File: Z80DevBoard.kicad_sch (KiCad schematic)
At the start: 83 parts, among them SW1 WAIT, SW2 RESET, SW3 Z80BOOT, SW4 RPBOOT

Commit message: Added the read data from ram hardware. Added resistors for leds and some diodes. Reorganized the spaces.
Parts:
- removed ShiftRegisterIn: 74HC165, symbol 74xx:74HC165
- added D11, D13, D15, D17, D19, D21, D23, D25, D27, D29, D3, D46, D5, D54, D56, D58, D59, D60, D61, D62, D63, D64, D7, D9: Diode, Diode_SMD:D_SOD-523, symbol Diode:1N4148WT
- added DataBus1, DataBus2: SN74LVC245APW, Package_SO:TSSOP-20_4.4x6.5mm_P0.65mm, symbol Logic_LevelTranslator:SN74LVC245APW
- added R19, R20, R21, R22, R23, R24, R25, R26, R27, R28, R29, R30, R31, R32, R33, R34, R35, R36, R37, R38, R39, R40, R41, R42, R43, R44, R45, R46, R47, R48, R49, R50, R51, R52: 220, Resistor_THT:R_Axial_DIN0207_L6.3mm_D2.5mm_P10.16mm_Horizontal, symbol Device:R
- added ShiftRegisterIn2: 74HC165, symbol 74xx:74HC165
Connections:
- net GND: now also DataBus1.10 (GND), DataBus2.10 (GND), ShiftRegisterIn2.8 (GND)
- net RAM-A0: now also DataBus.18 (B1)
- net RAM-A1: now also DataBus.17 (B2)
- net RAM-A10: now also DataBus1.16 (B3)
- net RAM-A11: now also DataBus1.15 (B4)
- net RAM-A12: now also DataBus1.14 (B5)
- net RAM-A13: now also DataBus1.13 (B6)
- net RAM-A14: now also DataBus1.12 (B7)
- net RAM-A2: now also DataBus.16 (B3)
- net RAM-A3: now also DataBus.15 (B4)
- net RAM-A4: now also DataBus.14 (B5)
- net RAM-A5: now also DataBus.13 (B6)
- net RAM-A6: now also DataBus.12 (B7)
- net RAM-A7: now also DataBus.11 (B8)
- net RAM-A8: now also DataBus1.18 (B1)
- net RAM-A9: now also DataBus1.17 (B2)
- net RAM-Q0: now also DataBus2.18 (B1), R22.2; no longer D31.2 (A), D32.1 (K)
- net RAM-Q1: now also DataBus2.17 (B2), R29.2; no longer D35.2 (A), D36.1 (K)
- net RAM-Q2: now also DataBus2.16 (B3), R30.2; no longer D39.2 (A), D40.1 (K)
- net RAM-Q3: now also DataBus2.15 (B4), R35.2; no longer D43.2 (A), D44.1 (K)
- net RAM-Q4: now also DataBus2.14 (B5), R23.2; no longer D47.2 (A), D48.1 (K)
- net RAM-Q5: now also DataBus2.13 (B6), R28.2; no longer D33.2 (A), D34.1 (K)
- net RAM-Q6: now also DataBus2.12 (B7), R31.2; no longer D37.2 (A), D38.1 (K)
- net RAM-Q7: now also DataBus2.11 (B8), R34.2; no longer D41.2 (A), D42.1 (K)
- net Vcc: now also DataBus1.20 (VCC), DataBus2.20 (VCC)
- net Vdd_3v3: now also ShiftRegisterIn2.16 (VCC)
- net Z80-A0: now also R40.2; no longer D8.2 (A)
- net Z80-A1: now also R41.2; no longer D22.2 (A)
- net Z80-A10: now also R38.2; no longer D12.2 (A)
- net Z80-A11: now also R43.2; no longer D14.2 (A)
- net Z80-A12: now also R46.2; no longer D16.2 (A)
- net Z80-A13: now also R49.2; no longer D18.2 (A)
- net Z80-A14: now also R52.2; no longer D20.2 (A)
- net Z80-A15: now also R19.1; no longer D57.2 (A)
- net Z80-A2: now also R44.2; no longer D26.2 (A)
- net Z80-A3: now also R47.2; no longer D28.2 (A)
- net Z80-A4: now also R50.2; no longer D30.2 (A)
- net Z80-A5: now also R39.2; no longer D10.2 (A)
- net Z80-A6: now also R42.2; no longer D2.2 (A)
- net Z80-A7: now also R45.2; no longer D4.2 (A)
- net Z80-A8: now also R48.2; no longer D6.2 (A)
- net Z80-A9: now also R51.2; no longer D24.2 (A)
- net Z80-D0: now also R25.1; no longer D31.1 (K), D32.2 (A)
- net Z80-D1: now also R26.1; no longer D35.1 (K), D36.2 (A)
- net Z80-D2: now also R32.1; no longer D39.1 (K), D40.2 (A)
- net Z80-D3: now also R36.1; no longer D43.1 (K), D44.2 (A)
- net Z80-D4: now also R24.1; no longer D47.1 (K), D48.2 (A)
- net Z80-D5: now also R27.1; no longer D33.1 (K), D34.2 (A)
- net Z80-D6: now also R33.1; no longer D37.1 (K), D38.2 (A)
- net Z80-D7: now also R37.1; no longer D41.1 (K), D42.2 (A)
- net Z80-RD: now also R20.1; no longer D49.2 (A)
- net Z80-WR: now also R21.1; no longer D55.2 (A)
- net at ShiftRegisterOut.1 (QB): now also D5.2 (A)
- net at ShiftRegisterOut.15 (QA): now also D3.2 (A)
- net at ShiftRegisterOut.2 (QC): now also D7.2 (A)
- net at ShiftRegisterOut.3 (QD): now also D9.2 (A)
- net at ShiftRegisterOut.4 (QE): now also D11.2 (A)
- net at ShiftRegisterOut.5 (QF): now also D13.2 (A)
- net at ShiftRegisterOut.6 (QG): now also D15.2 (A)
- net at ShiftRegisterOut.7 (QH): now also D17.2 (A)
- net at ShiftRegisterOut2.1 (QB): now also D61.2 (A)
- net at ShiftRegisterOut2.15 (QA): now also D56.2 (A)
- net at ShiftRegisterOut2.2 (QC): now also D58.2 (A)
- net at ShiftRegisterOut2.3 (QD): now also D62.2 (A)
- net at ShiftRegisterOut2.4 (QE): now also D59.2 (A)
- net at ShiftRegisterOut2.5 (QF): now also D63.2 (A)
- net at ShiftRegisterOut2.6 (QG): now also D60.2 (A)
- net at ShiftRegisterOut2.7 (QH): now also D64.2 (A)
- net at DataBus.2 (A1): now also D3.1 (K)
- net at DataBus.3 (A2): now also D5.1 (K)
- net at DataBus.4 (A3): now also D7.1 (K)
- net at DataBus.5 (A4): now also D9.1 (K)
- net at DataBus.6 (A5): now also D11.1 (K)
- net at DataBus.7 (A6): now also D13.1 (K)
- net at DataBus.8 (A7): now also D15.1 (K)
- net at DataBus.9 (A8): now also D17.1 (K)
- net at ShiftRegisterOut1.1 (QB): now also D27.2 (A)
- net at ShiftRegisterOut1.15 (QA): now also D19.2 (A)
- net at ShiftRegisterOut1.2 (QC): now also D21.2 (A)
- net at ShiftRegisterOut1.3 (QD): now also D29.2 (A)
- net at ShiftRegisterOut1.4 (QE): now also D23.2 (A)
- net at ShiftRegisterOut1.5 (QF): now also D46.2 (A)
- net at ShiftRegisterOut1.6 (QG): now also D25.2 (A)
- net at ShiftRegisterOut1.7 (QH): now also D54.2 (A)
- new net: D30.2 (A), R50.1
- new net: D19.1 (K), DataBus1.2 (A1)
- new net: D27.1 (K), DataBus1.3 (A2)
- new net: D21.1 (K), DataBus1.4 (A3)
- new net: D29.1 (K), DataBus1.5 (A4)
- new net: D23.1 (K), DataBus1.6 (A5)
- new net: D46.1 (K), DataBus1.7 (A6)
- new net: D25.1 (K), DataBus1.8 (A7)
- new net: D54.1 (K), DataBus1.9 (A8)
- new net: D37.2 (A), D38.1 (K), R31.1
- new net: D47.2 (A), D48.1 (K), R23.1
- new net: D43.2 (A), D44.1 (K), R35.1
- new net: D31.1 (K), D32.2 (A), R25.2
- new net: D31.2 (A), D32.1 (K), R22.1
- new net: D2.2 (A), R42.1
- new net: D28.2 (A), R47.1
- new net: D61.1 (K), DataBus2.3 (A2), ShiftRegisterIn2.12 (D1)
- new net: D41.1 (K), D42.2 (A), R37.2
- new net: D58.1 (K), DataBus2.4 (A3), ShiftRegisterIn2.13 (D2)
- new net: D56.1 (K), DataBus2.2 (A1), ShiftRegisterIn2.11 (D0)
- new net: D62.1 (K), DataBus2.5 (A4), ShiftRegisterIn2.14 (D3)
- new net: D59.1 (K), DataBus2.6 (A5), ShiftRegisterIn2.3 (D4)
- new net: D63.1 (K), DataBus2.7 (A6), ShiftRegisterIn2.4 (D5)
- new net: D60.1 (K), DataBus2.8 (A7), ShiftRegisterIn2.5 (D6)
- new net: D64.1 (K), DataBus2.9 (A8), ShiftRegisterIn2.6 (D7)
- new net: D39.1 (K), D40.2 (A), R32.2
- new net: D41.2 (A), D42.1 (K), R34.1
- new net: D26.2 (A), R44.1
- new net: D33.1 (K), D34.2 (A), R27.2
- new net: D33.2 (A), D34.1 (K), R28.1
- new net: D22.2 (A), R41.1
- new net: D24.2 (A), R51.1
- new net: D49.2 (A), R20.2
- new net: D37.1 (K), D38.2 (A), R33.2
- new net: D47.1 (K), D48.2 (A), R24.2
- new net: D8.2 (A), R40.1
- new net: D20.2 (A), R52.1
- new net: D4.2 (A), R45.1
- new net: D6.2 (A), R48.1
- new net: D55.2 (A), R21.2
- new net: D14.2 (A), R43.1
- new net: D39.2 (A), D40.1 (K), R30.1
- new net: D43.1 (K), D44.2 (A), R36.2
- new net: D12.2 (A), R38.1
- new net: D18.2 (A), R49.1
- new net: D10.2 (A), R39.1
- new net: D35.1 (K), D36.2 (A), R26.2
- new net: D35.2 (A), D36.1 (K), R29.1
- new net: D57.2 (A), R19.2
- new net: D16.2 (A), R46.1
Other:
- moved on the sheet: C3, C4, C5, C6, C7, C8, D1, D10, D12, D14, D16, D18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

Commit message: Added some footprints. Made the connections between the shift register and the RP2040.
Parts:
- C1, C2, C3, C4, C5, C6, C7, C8: footprint (none) -> Capacitor_SMD:CP_Elec_3x5.3
- F1: footprint (none) -> Fuse:Fuse_0402_1005Metric
- USB_C1: renamed from USB_C; footprint (none) -> Connector_USB:USB_C_Receptacle_Amphenol_124019772112A
- renumbered DataBus to DataBus3, LDO to LDO1, ShiftRegisterOut to ShiftRegisterOut3
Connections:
- net CLOCK: now also ShiftRegisterIn2.2 (CP)
- net GND: now also DataBus1.19 (~{OE}), DataBus2.19 (~{OE}), DataBus3.19 (~{OE}), ShiftRegisterIn2.15 (~{CE})
- net Vcc: now also DataBus1.1 (DIR), DataBus3.1 (DIR)
- net RP2040-RWRAM-GPIO5-DIR: now reaches DataBus2.1 (DIR)
- net RP2040-RWRAM-GPIO5-DIR: now also RP2040_1.7 (GPIO5)
- net RP2040-RWRAM-GPIO8-PL: now reaches RP2040_1.11 (GPIO8)
- net RP2040-RWRAM-GPIO8-PL: now also ShiftRegisterIn2.1 (~{PL})
- net RP2040-RWRAM-GPIO6-DS: now reaches RP2040_1.8 (GPIO6)
- net RP2040-RWRAM-GPIO6-DS: now also ShiftRegisterIn2.10 (DS)
- net RP2040-RWRAM-GPIO7-Q7: now reaches RP2040_1.9 (GPIO7)
- net RP2040-RWRAM-GPIO7-Q7: now also ShiftRegisterIn2.9 (Q7)
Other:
- moved on the sheet: RP2040_1

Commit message: Added the last footprints.
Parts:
- ShiftRegisterIn2, ShiftRegisterOut1, ShiftRegisterOut2, ShiftRegisterOut3: footprint (none) -> Package_DIP:DIP-16_W7.62mm
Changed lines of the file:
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@@
 			)
 		)
-		(property "Footprint" ""
+		(property "Footprint" "Package_DIP:DIP-16_W7.62mm"
 			(at 441.96 53.34 0)
 			(effects
@@
 			)
 		)
-		(property "Footprint" ""
+		(property "Footprint" "Package_DIP:DIP-16_W7.62mm"
 			(at 441.96 198.12 0)
 			(effects
@@
 			)
 		)
-		(property "Footprint" ""
+		(property "Footprint" "Package_DIP:DIP-16_W7.62mm"
 			(at 441.96 125.73 0)
 			(effects
@@
 			)
 		)
-		(property "Footprint" ""
+		(property "Footprint" "Package_DIP:DIP-16_W7.62mm"
 			(at 502.92 200.66 0)
 			(effects

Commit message: Updated the USB C port.
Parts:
- USB_C1: footprint Connector_USB:USB_C_Receptacle_Amphenol_124019772112A -> Connector_USB:USB_C_Receptacle_GCT_USB4085
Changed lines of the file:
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@@
 			)
 		)
-		(property "Footprint" "Connector_USB:USB_C_Receptacle_Amphenol_124019772112A"
+		(property "Footprint" "Connector_USB:USB_C_Receptacle_GCT_USB4085"
 			(at 528.32 344.17 0)
 			(effects

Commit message: Fixed the oscillators. Fixed the crystal. Fixed the connections between the RP2040 and the Flash. Updated README.
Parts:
- removed R16: 10k, Resistor_THT:R_Axial_DIN0207_L6.3mm_D2.5mm_P10.16mm_Horizontal, symbol Device:R
- added C10, C12, C9: 0.1uF, Capacitor_SMD:CP_Elec_3x5.3, symbol Device:C
- added C11: 12pF, Capacitor_SMD:CP_Elec_3x5.3, symbol Device:C
- added J1: Conn_01x02_MountingPin, Connector_PinHeader_1.00mm:PinHeader_1x02_P1.00mm_Vertical, symbol Connector_Generic_MountingPin:Conn_01x02_MountingPin
- added O2: 10KHz, Oscillator:Oscillator_SMD_SeikoEpson_SG210-4Pin_2.5x2.0mm, symbol Device:Oscilloscope
- added Y1: Crystal, Crystal:Crystal_HC49-4H_Vertical, symbol Device:Crystal
- C8: value 0.1uF -> 12pF
- O1: value 6MHz -> 10KHz; footprint Crystal:Crystal_HC49-4H_Vertical -> Oscillator:Oscillator_SMD_SeikoEpson_SG210-4Pin_2.5x2.0mm
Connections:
- net FLASH-HOLD/RESET is gone; now on net FLASH-HOLD-RESRT-RP2040-QSPI_SD3: Flash1.7 (~{HOLD}/~{RESET}/IO_{3})
- net GND: now also C11.1, C12.1, C9.1, J1.MP (MountPin)
- net Vdd_3v3: now also C10.2, C12.2, C9.2, O2.2 (+); no longer C8.2
- net RP2040_XOUT: now reaches RP2040_1.21 (XOUT)
- net RP2040_XOUT: now also C11.2, Y1.2
- net RP2040-SWCLK-PIN: now reaches RP2040_1.24 (SWCLK)
- net RP2040-SWCLK-PIN: now also J1.1 (Pin_1)
- net RP2040-SWD-PIN: now reaches RP2040_1.25 (SWD)
- net RP2040-SWD-PIN: now also J1.2 (Pin_2)
- net Vcc-RP2040-RUN: now reaches RP2040_1.26 (RUN)
- net Vcc-RP2040-RUN: now also R15.1
- net RP2040-VREG_IN: now reaches RP2040_1.44 (VREG_IN)
- net RP2040-VREG_IN: now also C10.1
- net FLASH-HOLD-RESRT-RP2040-QSPI_SD3: now reaches RP2040_1.51 (QSPI_SD3)
- net FLASH-WP-RP2040-QSPI_SD2: now reaches RP2040_1.54 (QSPI_SD2)
- net FLASH-WP-RP2040-QSPI_SD2: now also Flash1.3 (~{WP}/IO_{2})
- net CLOCK renamed CLOCK_BUS
- net CLOCK_BUS: no longer Flash1.6 (CLK), RP2040_1.20 (XIN), RP2040_1.52 (QSPI_SCLK), Z80.6 (CLK)
- removed net FLASH-WP: Flash1.3 (~{WP}/IO_{2}), R15.1
- new net CLOCK_FLASH: Flash1.6 (CLK), RP2040_1.52 (QSPI_SCLK)
- new net CLOCK_Z80: O2.1 (-), Z80.6 (CLK)
- new net RP2040_XIN: C8.2, RP2040_1.20 (XIN), Y1.1
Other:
- note added: "Pins"
- moved on the sheet: C3, C4, C5, C6, C8, R1, R12, R13, R2, R3, RAM1

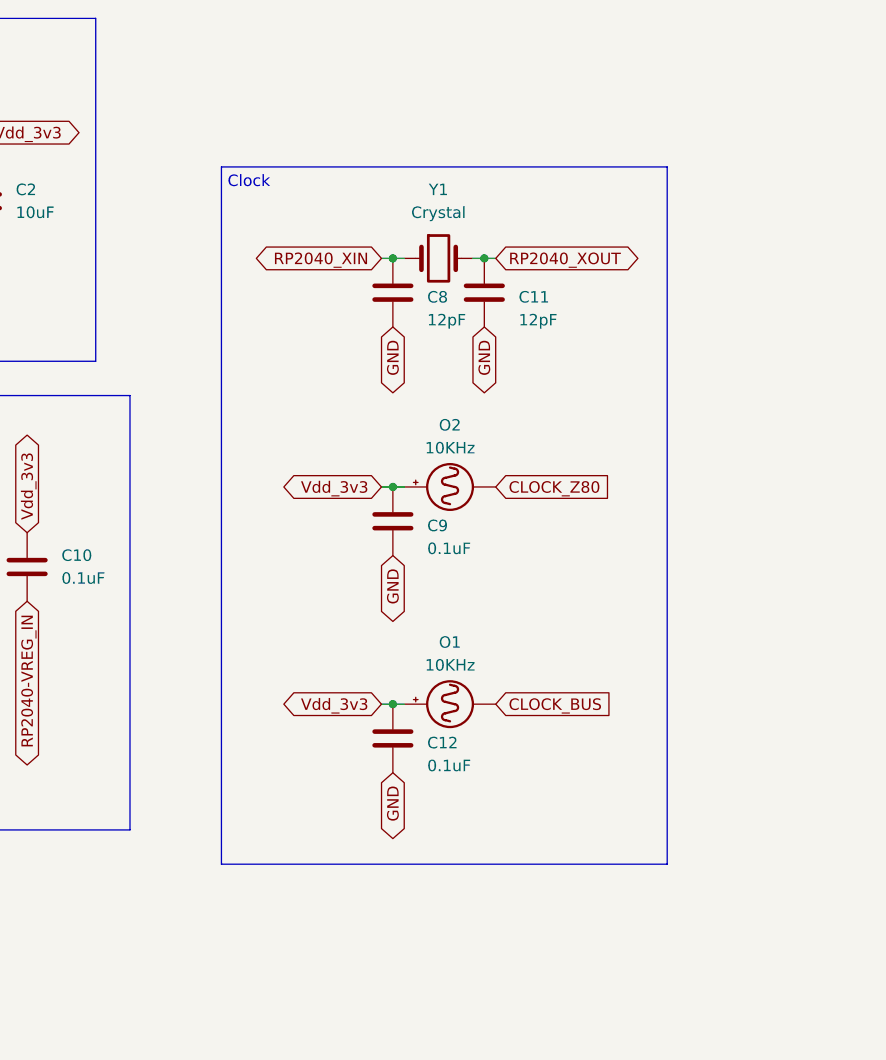
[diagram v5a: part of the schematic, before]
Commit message: Added the manual clock for the Z80. Fixed all the components. Started fixing some connections.
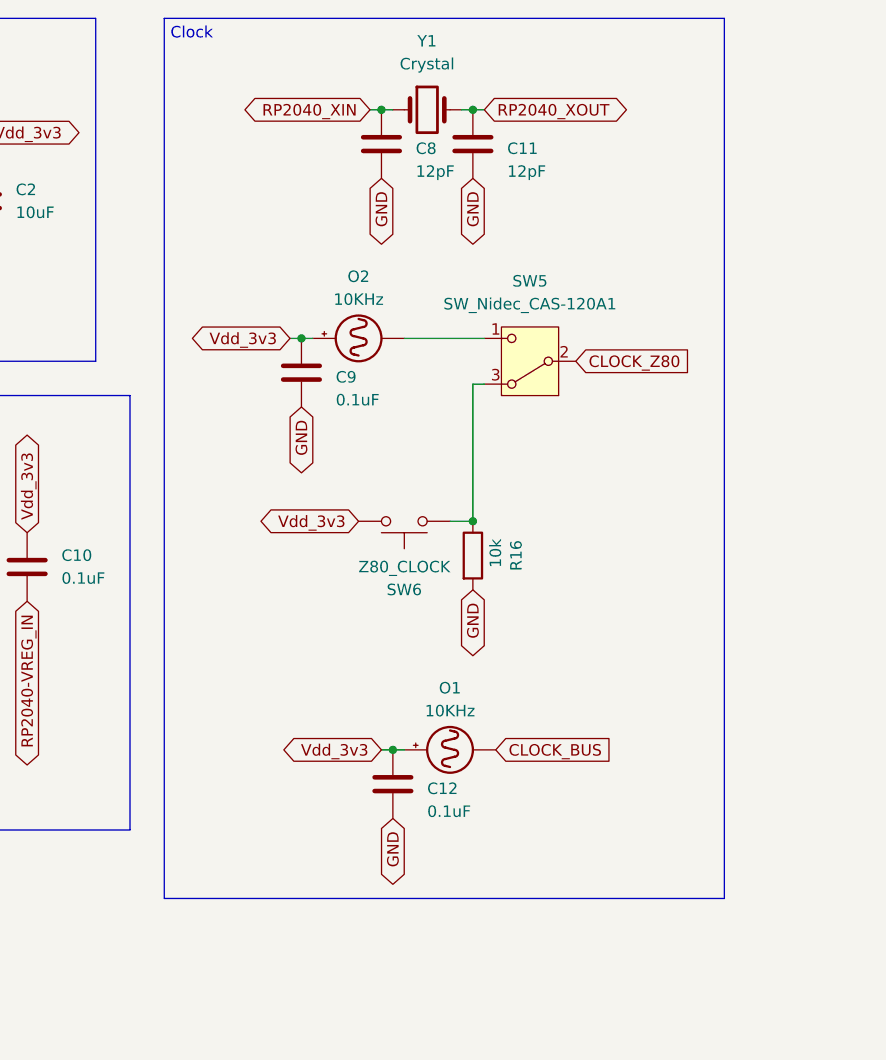
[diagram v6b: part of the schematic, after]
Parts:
- added R16: 10k, Resistor_THT:R_Axial_DIN0207_L6.3mm_D2.5mm_P10.16mm_Horizontal, symbol Device:R
- added SW5: SW_Nidec_CAS-120A1, Button_Switch_SMD:Nidec_Copal_CAS-120A, symbol Switch:SW_Nidec_CAS-120A1
- added SW6: Z80_CLOCK, Button_Switch_THT:SW_PUSH_6mm_H7.3mm, symbol Switch:SW_Push
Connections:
- net CLOCK_Z80: now also SW5.2 (B); no longer O2.1 (-)
- net GND: now also R16.2
- net Vdd_3v3: now also SW6.1
- new net: O2.1 (-), SW5.1 (C)
- new net: R16.1, SW5.3 (A), SW6.2
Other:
- moved on the sheet: C11, C12, C8, C9, O1, O2, Y1

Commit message: Added the debouncer. Fixed the board sizes.
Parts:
- added C13: 0.1uF, Capacitor_SMD:CP_Elec_3x5.3, symbol Device:C
- added R53: 10k, Resistor_THT:R_Axial_DIN0207_L6.3mm_D2.5mm_P10.16mm_Horizontal, symbol Device:R
- added U1: 74HC14, Package_DIP:DIP-14_W7.62mm, symbol 74xx:74HC14
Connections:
- net GND: now also SW6.1, C13.1, U1.7 (GND); no longer R16.2
- net Vdd_3v3: now also R16.2, U1.14 (VCC); no longer SW6.1
- net at R16.1, SW6.2: now also R53.1; no longer SW5.3 (A)
- new net: C13.2, R53.2, U1.1
- new net Z80_MANUAL_CLOCK: SW5.3 (A), U1.2
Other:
- note added: "Debouncer"
- moved on the sheet: C12, O1, R16, SW6

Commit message: Changed the footprint of the capacitors.
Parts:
- C1, C10, C11, C12, C13, C2, C3, C4, C5, C6, C7, C8, C9: footprint Capacitor_SMD:CP_Elec_3x5.3 -> Capacitor_THT:CP_Radial_D4.0mm_P1.50mm
- U1: footprint (none) -> Package_DIP:DIP-14_W7.62mm
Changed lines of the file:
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@@
 			)
 		)
-		(property "Footprint" "Capacitor_SMD:CP_Elec_3x5.3"
+		(property "Footprint" "Capacitor_THT:CP_Radial_D4.0mm_P1.50mm"
 			(at 110.7948 25.4 0)
 			(effects
@@
 			)
 		)
-		(property "Footprint" "Capacitor_SMD:CP_Elec_3x5.3"
+		(property "Footprint" "Capacitor_THT:CP_Radial_D4.0mm_P1.50mm"
 			(at 20.6248 72.39 0)
 			(effects
@@
 			)
 		)
-		(property "Footprint" "Capacitor_SMD:CP_Elec_3x5.3"
+		(property "Footprint" "Capacitor_THT:CP_Radial_D4.0mm_P1.50mm"
 			(at 43.4848 31.75 0)
 			(effects
@@
 			)
 		)
-		(property "Footprint" "Capacitor_SMD:CP_Elec_3x5.3"
+		(property "Footprint" "Capacitor_THT:CP_Radial_D4.0mm_P1.50mm"
 			(at 103.1748 275.59 0)
 			(effects
@@
 			)
 		)
-		(property "Footprint" "Capacitor_SMD:CP_Elec_3x5.3"
+		(property "Footprint" "Capacitor_THT:CP_Radial_D4.0mm_P1.50mm"
 			(at 71.4248 72.39 0)
 			(effects
@@
 			)
 		)
-		(property "Footprint" "Capacitor_SMD:CP_Elec_3x5.3"
+		(property "Footprint" "Capacitor_THT:CP_Radial_D4.0mm_P1.50mm"
 			(at 66.3448 31.75 0)
 			(effects
@@
 			)
 		)
-		(property "Footprint" ""
+		(property "Footprint" "Package_DIP:DIP-14_W7.62mm"
 			(at 424.18 344.17 0)
 			(effects
@@
 			)
 		)
-		(property "Footprint" "Capacitor_SMD:CP_Elec_3x5.3"
+		(property "Footprint" "Capacitor_THT:CP_Radial_D4.0mm_P1.50mm"
 			(at 376.2248 336.55 0)
 			(effects
@@
 			)
 		)
-		(property "Footprint" "Capacitor_SMD:CP_Elec_3x5.3"
+		(property "Footprint" "Capacitor_THT:CP_Radial_D4.0mm_P1.50mm"
 			(at 101.9048 50.8 0)
 			(effects
@@
 			)
 		)
-		(property "Footprint" "Capacitor_SMD:CP_Elec_3x5.3"
+		(property "Footprint" "Capacitor_THT:CP_Radial_D4.0mm_P1.50mm"
 			(at 110.7948 91.44 0)
 			(effects
@@
 			)
 		)
-		(property "Footprint" "Capacitor_SMD:CP_Elec_3x5.3"
+		(property "Footprint" "Capacitor_THT:CP_Radial_D4.0mm_P1.50mm"
 			(at 32.0548 72.39 0)
 			(effects
@@
 			)
 		)
-		(property "Footprint" "Capacitor_SMD:CP_Elec_3x5.3"
+		(property "Footprint" "Capacitor_THT:CP_Radial_D4.0mm_P1.50mm"
 			(at 44.7548 72.39 0)
 			(effects
@@
 			)
 		)
-		(property "Footprint" "Capacitor_SMD:CP_Elec_3x5.3"
+		(property "Footprint" "Capacitor_THT:CP_Radial_D4.0mm_P1.50mm"
 			(at 57.4548 72.39 0)
 			(effects
@@
 			)
 		)
-		(property "Footprint" "Capacitor_SMD:CP_Elec_3x5.3"
+		(property "Footprint" "Capacitor_THT:CP_Radial_D4.0mm_P1.50mm"
 			(at 120.9548 25.4 0)
 			(effects
